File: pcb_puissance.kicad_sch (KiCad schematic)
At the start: 38 parts, among them J1 1755736, J10 Conn_01x02, J11 Conn_01x02, J2 1755736, J3 1755736, J4 1755736, J5 1755736, J6 1755736, J7 1755736, J8 1755736, J9 Conn_01x02, K1 SRD-05VDC-SL-C

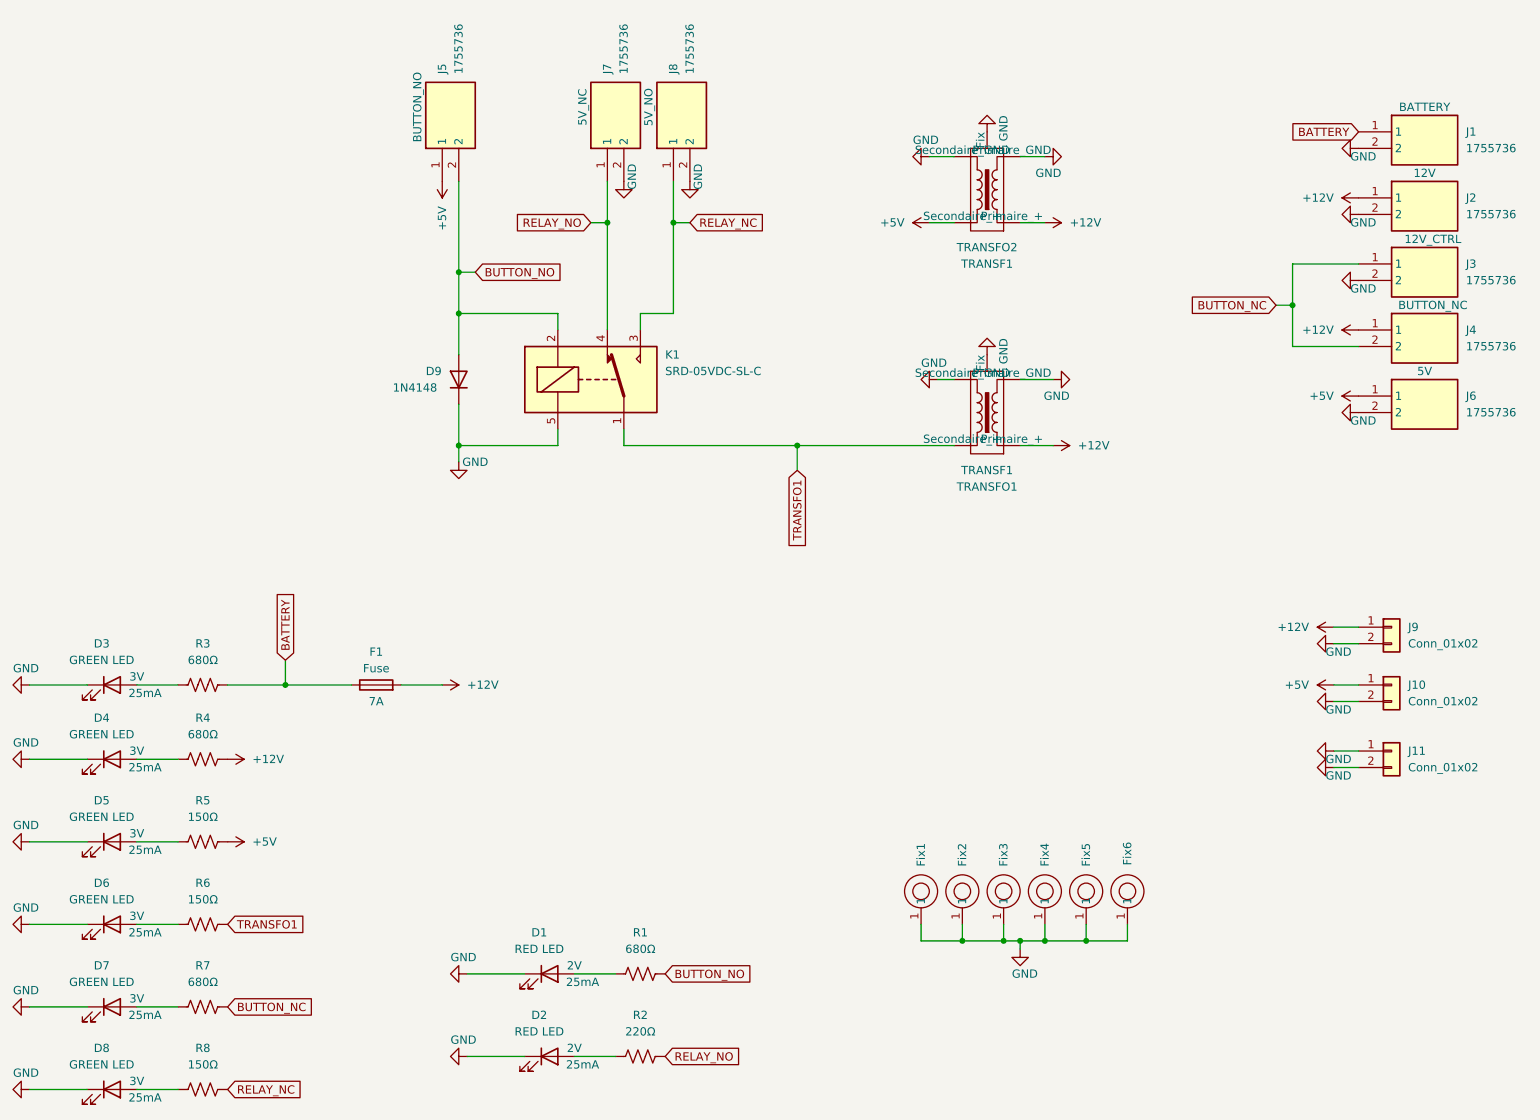
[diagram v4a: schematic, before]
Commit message: Rectification empreinte relai
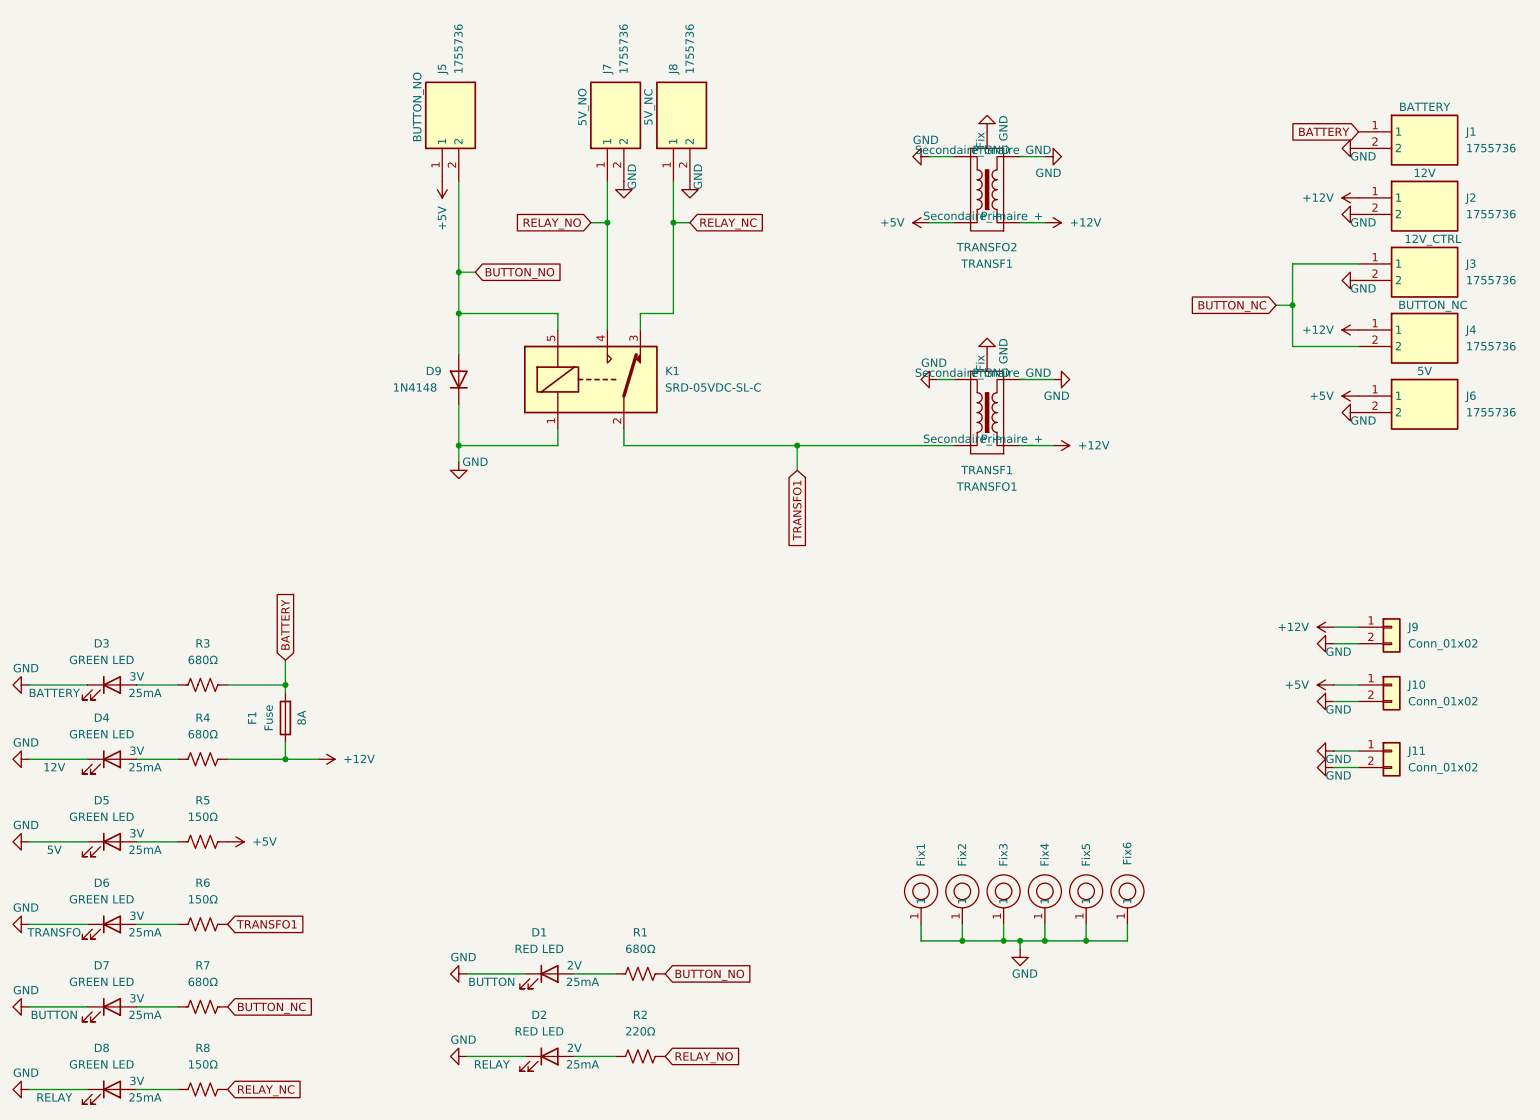
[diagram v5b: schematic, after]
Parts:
- removed K1: SRD-05VDC-SL-C, Relay_THT:Relay_SPDT_SANYOU_SRD_Series_Form_C, symbol Relay:G5Q-1
- added K1: SRD-05VDC-SL-C, Library:SRD-05VDC-SL-C, symbol New_Library:SRD-05VDC-SL-C
- F1: In 7A -> 8A
- J7: Name 5V_NC -> 5V_NO
- J8: Name 5V_NO -> 5V_NC
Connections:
- net +12V: now also F1.1; no longer F1.2
- net BATTERY: now also F1.2; no longer F1.1
- net BUTTON_NO: now also K1.5
- net GND: now also K1.1
- net RELAY_NC: now also K1.3
- net RELAY_NO: now also K1.4
- net TRANSFO1: now also K1.2
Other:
- moved on the sheet: F1
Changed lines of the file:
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@@
     (company "Modelec")
   )
+  (junction (at 81.28 130.81) (diameter 0) (color 0 0 0 0)
+  )
   (junction (at 236.22 60.96) (diameter 0) (color 0 0 0 0)
   )
@@
   (junction (at 198.12 158.75) (diameter 0) (color 0 0 0 0)
   )
+  (junction (at 81.28 119.38) (diameter 0) (color 0 0 0 0)
+  )
   (junction (at 185.42 158.75) (diameter 0) (color 0 0 0 0)
   )
-  (junction (at 81.28 119.38) (diameter 0) (color 0 0 0 0)
-  )
   (junction (at 160.02 82.55) (diameter 0) (color 0 0 0 0)
   )
@@
     (stroke (width 0) (type default))
   )
+  (wire (pts (xy 81.28 119.38) (xy 81.28 120.65))
+    (stroke (width 0) (type default))
+  )
   (wire (pts (xy 160.02 82.55) (xy 133.35 82.55))
     (stroke (width 0) (type default))
@@
     (stroke (width 0) (type default))
   )
+  (wire (pts (xy 81.28 128.27) (xy 81.28 130.81))
+    (stroke (width 0) (type default))
+  )
   (wire (pts (xy 242.57 113.03) (xy 246.38 113.03))
     (stroke (width 0) (type default))
   )
+  (wire (pts (xy 81.28 130.81) (xy 86.36 130.81))
+    (stroke (width 0) (type default))
+  )
   (wire (pts (xy 109.22 176.53) (xy 118.11 176.53))
     (stroke (width 0) (type default))
@@
     (stroke (width 0) (type default))
   )
-  (wire (pts (xy 105.41 119.38) (xy 99.06 119.38))
+  (wire (pts (xy 72.39 130.81) (xy 81.28 130.81))
     (stroke (width 0) (type default))
   )
   (wire (pts (xy 194.31 82.55) (xy 199.39 82.55))
-    (stroke (width 0) (type default))
-  )
-  (wire (pts (xy 81.28 119.38) (xy 91.44 119.38))
     (stroke (width 0) (type default))
   )
@@
     )
   )
-  (symbol (lib_id "Device:Fuse") (at 95.25 119.38 90) (unit 1)
-    (in_bom yes) (on_board yes) (dnp no)
-    (property "Reference" "F1" (at 95.25 114.3 90)
-      (effects (font (size 1.27 1.27)))
-    )
-    (property "Value" "Fuse" (at 95.25 116.84 90)
-      (effects (font (size 1.27 1.27)))
-    )
-    (property "Footprint" "Library:porte fusible E44" (at 95.25 121.158 90)
-      (effects (font (size 1.27 1.27)) hide)
-    )
-    (property "Datasheet" "~" (at 95.25 119.38 0)
-      (effects (font (size 1.27 1.27)) hide)
-    )
-    (property "In" "7A" (at 95.25 121.92 90)
+  (symbol (lib_id "Device:Fuse") (at 81.28 124.46 180) (unit 1)
+    (in_bom yes) (on_board yes) (dnp no)
+    (property "Reference" "F1" (at 76.2 124.46 90)
+      (effects (font (size 1.27 1.27)))
+    )
+    (property "Value" "Fuse" (at 78.74 124.46 90)
+      (effects (font (size 1.27 1.27)))
+    )
+    (property "Footprint" "Library:porte fusible E44" (at 83.058 124.46 90)
+      (effects (font (size 1.27 1.27)) hide)
+    )
+    (property "Datasheet" "~" (at 81.28 124.46 0)
+      (effects (font (size 1.27 1.27)) hide)
+    )
+    (property "In" "8A" (at 83.82 124.46 90)
       (effects (font (size 1.27 1.27)))
     )
@@
     )
   )
-  (symbol (lib_id "power:+12V") (at 105.41 119.38 270) (unit 1)
-    (in_bom yes) (on_board yes) (dnp no) (fields_autoplaced)
-    (property "Reference" "#PWR028" (at 101.6 119.38 0)
-      (effects (font (size 1.27 1.27)) hide)
-    )
-    (property "Value" "+12V" (at 109.22 119.38 90)
-      (effects (font (size 1.27 1.27)) (justify left))
-    )
-    (property "Footprint" "" (at 105.41 119.38 0)
-      (effects (font (size 1.27 1.27)) hide)
-    )
-    (property "Datasheet" "" (at 105.41 119.38 0)
-      (effects (font (size 1.27 1.27)) hide)
-    )
-    (pin "1")
-    (instances
-      (project "pcb_puissance"
-        (path "/e9cf362a-cefc-43a9-90ea-df8ba9531768"
-          (reference "#PWR028") (unit 1)
-        )
-      )
-    )
-  )
   (symbol (lib_id "Device:LED") (at 54.61 119.38 0) (unit 1)
     (in_bom yes) (on_board yes) (dnp no)
@@
       (effects (font (size 1.27 1.27)))
     )
-    (property "Name" "BATTERY" (at 54.61 119.38 0)
-      (effects (font (size 1.27 1.27)) hide)
+    (property "Name" "BATTERY" (at 45.72 120.65 0)
+      (effects (font (size 1.27 1.27)))
     )
     (pin "1")
@@
       (effects (font (size 1.27 1.27)))
     )
-    (property "Name" "RELAY" (at 121.92 176.53 0)
-      (effects (font (size 1.27 1.27)) hide)
+    (property "Name" "RELAY" (at 113.03 177.8 0)
+      (effects (font (size 1.27 1.27)))
     )
     (pin "1")
@@
         (path "/e9cf362a-cefc-43a9-90ea-df8ba9531768"
           (reference "J2") (unit 1)
-        )
-      )
-    )
-  )
-  (symbol (lib_id "Relay:G5Q-1") (at 128.27 72.39 0) (unit 1)
-    (in_bom yes) (on_board yes) (dnp no)
-    (property "Reference" "K1" (at 139.7 68.58 0)
-      (effects (font (size 1.27 1.27)) (justify left))
-    )
-    (property "Value" "SRD-05VDC-SL-C" (at 139.7 71.12 0)
-      (effects (font (size 1.27 1.27)) (justify left))
-    )
-    (property "Footprint" "Relay_THT:Relay_SPDT_SANYOU_SRD_Series_Form_C" (at 139.7 73.66 0)
-      (effects (font (size 1.27 1.27)) (justify left) hide)
-    )
-    (property "Datasheet" "https://www.lcsc.com/product-detail/Power-Relays_Ningbo-Songle-Relay-SRD-05VDC-SL-C_C35449.html" (at 139.7 76.2 0)
-      (effects (font (size 1.27 1.27)) (justify left) hide)
-    )
-    (pin "4")
-    (pin "2")
-    (pin "5")
-    (pin "1")
-    (pin "3")
-    (instances
-      (project "pcb_puissance"
-        (path "/e9cf362a-cefc-43a9-90ea-df8ba9531768"
-          (reference "K1") (unit 1)
         )
       )
@@
       (effects (font (size 1.27 1.27)))
     )
-    (property "Name" "BUTTON" (at 54.61 168.91 0)
-      (effects (font (size 1.27 1.27)) hide)
+    (property "Name" "BUTTON" (at 45.72 170.18 0)
+      (effects (font (size 1.27 1.27)))
     )
     (pin "1")
@@
       (effects (font (size 1.27 1.27)))
     )
-    (property "Name" "RELAY" (at 54.61 181.61 0)
-      (effects (font (size 1.27 1.27)) hide)
+    (property "Name" "RELAY" (at 45.72 182.88 0)
+      (effects (font (size 1.27 1.27)))
     )
     (pin "1")
@@
       (effects (font (size 1.27 1.27)))
     )
-    (property "Name" "TRANSFO" (at 54.61 156.21 0)
-      (effects (font (size 1.27 1.27)) hide)
+    (property "Name" "TRANSFO" (at 45.72 157.48 0)
+      (effects (font (size 1.27 1.27)))
     )
     (pin "1")
@@
       (effects (font (size 1.27 1.27)))
     )
-    (property "Name" "12V" (at 54.61 130.81 0)
-      (effects (font (size 1.27 1.27)) hide)
+    (property "Name" "12V" (at 45.72 132.08 0)
+      (effects (font (size 1.27 1.27)))
     )
     (pin "1")
@@
     )
   )
-  (symbol (lib_id "power:+12V") (at 72.39 130.81 270) (unit 1)
-    (in_bom yes) (on_board yes) (dnp no) (fields_autoplaced)
-    (property "Reference" "#PWR010" (at 68.58 130.81 0)
-      (effects (font (size 1.27 1.27)) hide)
-    )
-    (property "Value" "+12V" (at 76.2 130.81 90)
-      (effects (font (size 1.27 1.27)) (justify left))
-    )
-    (property "Footprint" "" (at 72.39 130.81 0)
-      (effects (font (size 1.27 1.27)) hide)
-    )
-    (property "Datasheet" "" (at 72.39 130.81 0)
+  (symbol (lib_id "power:+12V") (at 86.36 130.81 270) (unit 1)
+    (in_bom yes) (on_board yes) (dnp no) (fields_autoplaced)
+    (property "Reference" "#PWR010" (at 82.55 130.81 0)
+      (effects (font (size 1.27 1.27)) hide)
+    )
+    (property "Value" "+12V" (at 90.17 130.81 90)
+      (effects (font (size 1.27 1.27)) (justify left))
+    )
+    (property "Footprint" "" (at 86.36 130.81 0)
+      (effects (font (size 1.27 1.27)) hide)
+    )
+    (property "Datasheet" "" (at 86.36 130.81 0)
       (effects (font (size 1.27 1.27)) hide)
     )
@@
       (effects (font (size 1.27 1.27)))
     )
-    (property "Name" "5V" (at 54.61 143.51 0)
-      (effects (font (size 1.27 1.27)) hide)
+    (property "Name" "5V" (at 45.72 144.78 0)
+      (effects (font (size 1.27 1.27)))
     )
     (pin "1")
@@
     )
   )
+  (symbol (lib_id "New_Library:SRD-05VDC-SL-C") (at 128.27 72.39 0) (unit 1)
+    (in_bom yes) (on_board yes) (dnp no) (fields_autoplaced)
+    (property "Reference" "K1" (at 139.7 71.12 0)
+      (effects (font (size 1.27 1.27)) (justify left))
+    )
+    (property "Value" "SRD-05VDC-SL-C" (at 139.7 73.66 0)
+      (effects (font (size 1.27 1.27)) (justify left))
+    )
+    (property "Footprint" "Library:SRD-05VDC-SL-C" (at 139.7 73.66 0)
+      (effects (font (size 1.27 1.27)) (justify left) hide)
+    )
+    (property "Datasheet" "http://www.songlerelay.com/Product_show_id_212.htm" (at 128.27 72.39 0)
+      (effects (font (size 1.27 1.27)) (justify left) hide)
+    )
+    (pin "1")
+    (pin "2")
+    (pin "3")
+    (pin "4")
+    (pin "5")
+    (instances
+      (project "pcb_puissance"
+        (path "/e9cf362a-cefc-43a9-90ea-df8ba9531768"
+          (reference "K1") (unit 1)
+        )
+      )
+    )
+  )
   (symbol (lib_id "power:GND") (at 41.91 156.21 270) (unit 1)
     (in_bom yes) (on_board yes) (dnp no)
@@
       (effects (font (size 1.27 1.27)))
     )
-    (property "Name" "BUTTON" (at 121.92 163.83 0)
-      (effects (font (size 1.27 1.27)) hide)
+    (property "Name" "BUTTON" (at 113.03 165.1 0)
+      (effects (font (size 1.27 1.27)))
     )
     (pin "1")
@@
       (effects (font (size 1.27 1.27)) (justify left top) hide)
     )
-    (property "Name" "5V_NO" (at 137.16 30.48 0)
+    (property "Name" "5V_NC" (at 137.16 30.48 0)
       (effects (font (size 1.27 1.27)))
     )
@@
       (effects (font (size 1.27 1.27)) (justify left top) hide)
     )
-    (property "Name" "5V_NC" (at 127 30.48 0)
-      (effects (font (size 1.27 1.27)))
-    )
+    (property "Name" "5V_NO" (at 127 30.48 0)
+      (effects (font (size 1.27 1.27)))
+    )

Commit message: Correctifs version 1.2
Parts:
- R2: value 220Ω -> 1.6kΩ
- R3, R4, R7: value 680Ω -> 1.5kΩ
- R5, R6, R8: value 150Ω -> 360Ω
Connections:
- net BUTTON_NO: now also D9.1 (K); no longer D9.2 (A)
- net GND: now also D9.2 (A); no longer D9.1 (K)
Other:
- moved on the sheet: D9
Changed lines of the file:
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@@
   (title_block
     (title "Carte de puissance")
-    (date "2023-11-30")
-    (rev "1.1")
+    (date "2024-03-18")
+    (rev "1.2")
     (company "Modelec")
   )
@@
       (effects (font (size 1.27 1.27)) hide)
     )
-    (property "Datasheet" "~" (at 81.28 124.46 0)
+    (property "Datasheet" "https://www.e44.com/composants/composants-passifs/fusibles-protections/porte-fusibles/porte-fusibles-ci/support-fusible-ci-5-20mm-vertical-SF5CIV.html" (at 81.28 124.46 0)
       (effects (font (size 1.27 1.27)) hide)
     )
@@
       (effects (font (size 1.27 1.27)))
     )
-    (property "Value" "150Ω" (at 68.58 177.8 90)
+    (property "Value" "360Ω" (at 68.58 177.8 90)
       (effects (font (size 1.27 1.27)))
     )
@@
     )
   )
-  (symbol (lib_id "Diode:1N4148") (at 107.95 72.39 90) (unit 1)
-    (in_bom yes) (on_board yes) (dnp no)
-    (property "Reference" "D9" (at 102.87 71.12 90)
+  (symbol (lib_id "Diode:1N4148") (at 107.95 72.39 270) (unit 1)
+    (in_bom yes) (on_board yes) (dnp no)
+    (property "Reference" "D9" (at 100.33 73.66 90)
       (effects (font (size 1.27 1.27)) (justify right))
     )
-    (property "Value" "1N4148" (at 97.79 73.66 90)
+    (property "Value" "1N4148" (at 105.41 71.12 90)
       (effects (font (size 1.27 1.27)) (justify right))
     )
@@
       (effects (font (size 1.27 1.27)) hide)
     )
-    (property "Datasheet" "" (at 189.23 77.47 0)
+    (property "Datasheet" "https://www.amazon.fr/Supernight-Convertisseurs-Transformer-Adjustable-Electricity/dp/B079N8HCHB/ref=sr_1_5" (at 189.23 77.47 0)
       (effects (font (size 1.27 1.27)) hide)
     )
@@
       (effects (font (size 1.27 1.27)))
     )
-    (property "Value" "680Ω" (at 68.58 165.1 90)
+    (property "Value" "1.5kΩ" (at 68.58 165.1 90)
       (effects (font (size 1.27 1.27)))
     )
@@
       (effects (font (size 1.27 1.27)))
     )
-    (property "Value" "680Ω" (at 68.58 115.57 90)
+    (property "Value" "1.5kΩ" (at 68.58 115.57 90)
       (effects (font (size 1.27 1.27)))
     )
@@
       (effects (font (size 1.27 1.27)))
     )
-    (property "Value" "220Ω" (at 135.89 172.72 90)
+    (property "Value" "1.6kΩ" (at 135.89 172.72 90)
       (effects (font (size 1.27 1.27)))
     )
@@
       (effects (font (size 1.27 1.27)) hide)
     )
-    (property "Datasheet" "" (at 189.23 43.18 0)
+    (property "Datasheet" "https://www.amazon.fr/Supernight-Convertisseurs-Transformer-Adjustable-Electricity/dp/B079N8HCHB/ref=sr_1_5" (at 189.23 43.18 0)
       (effects (font (size 1.27 1.27)) hide)
     )
@@
       (effects (font (size 1.27 1.27)))
     )
-    (property "Value" "680Ω" (at 68.58 127 90)
+    (property "Value" "1.5kΩ" (at 68.58 127 90)
       (effects (font (size 1.27 1.27)))
     )
@@
       (effects (font (size 1.27 1.27)))
     )
-    (property "Value" "150Ω" (at 68.58 139.7 90)
+    (property "Value" "360Ω" (at 68.58 139.7 90)
       (effects (font (size 1.27 1.27)))
     )
@@
       (effects (font (size 1.27 1.27)))
     )
-    (property "Value" "150Ω" (at 68.58 152.4 90)
-      (effects (font (size 1.27 1.27)))
-    )
+    (property "Value" "360Ω" (at 68.58 152.4 90)
+      (effects (font (size 1.27 1.27)))
+    )
